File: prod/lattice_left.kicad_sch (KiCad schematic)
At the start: 83 parts, among them J1 USB_C_Receptacle, J2 USB_C_Receptacle, SW1 SW_Push, SW2 SW_Push, U1 XC6206PxxxMR, U2 USBLC6-2SC6, U3 W25Q128JVS, U4 RP2040, Y1 12MHz

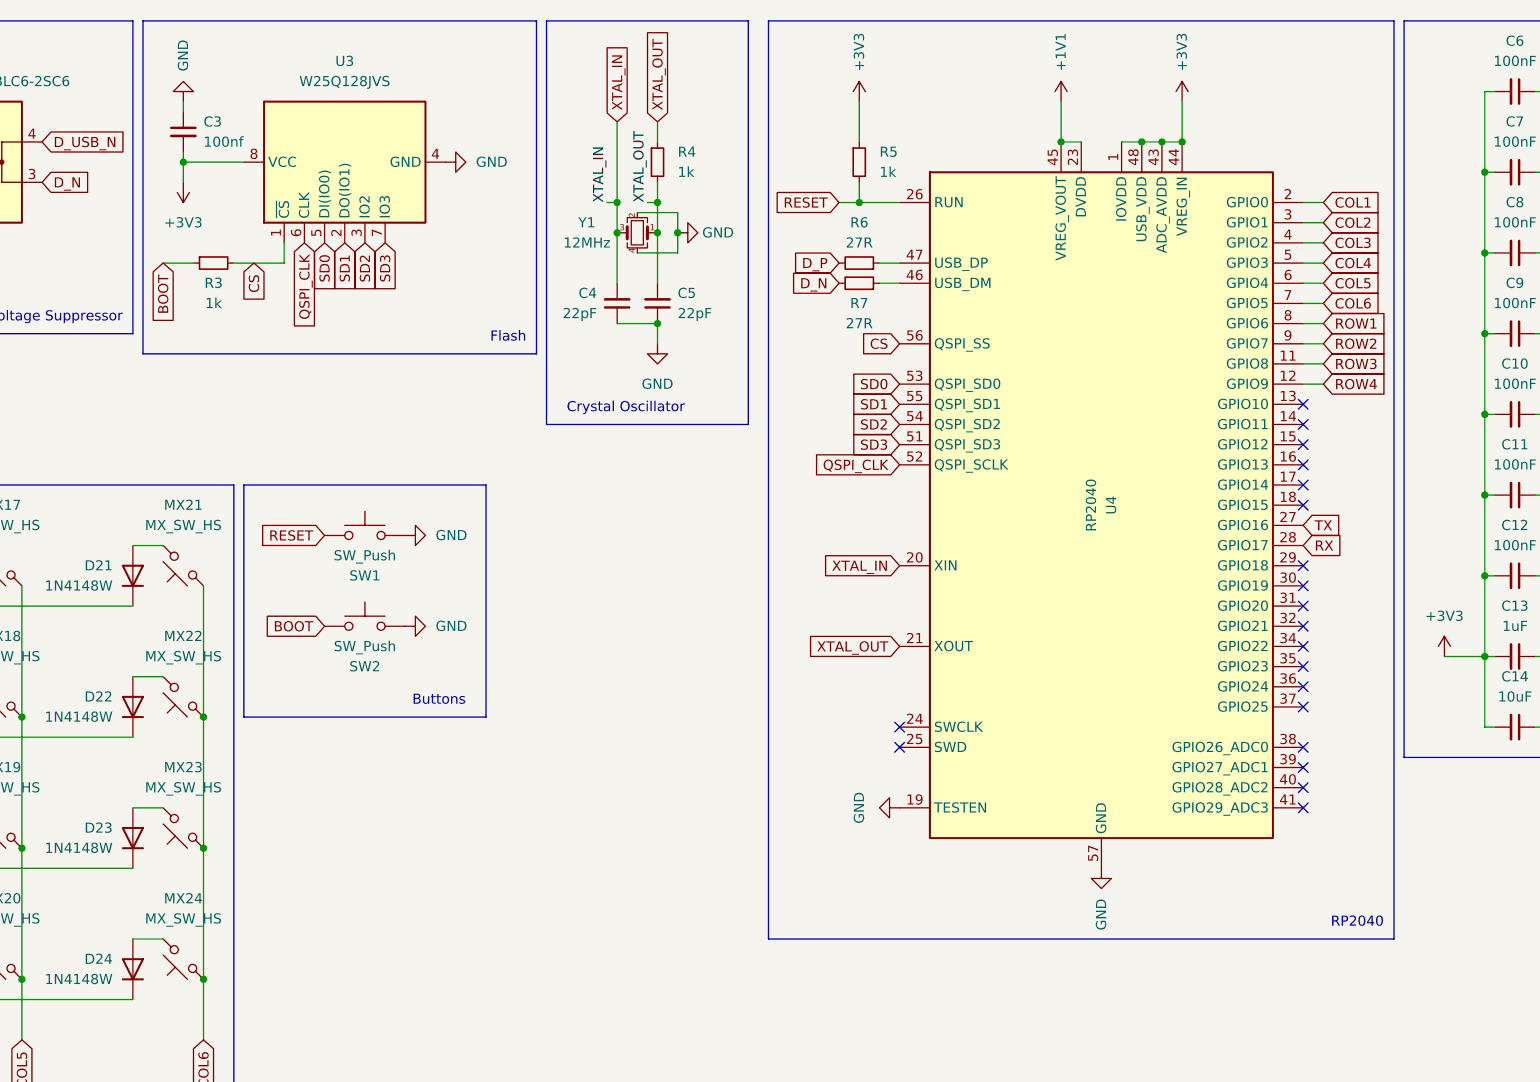
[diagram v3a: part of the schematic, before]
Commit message: component placement (swap rp2040 and flash)
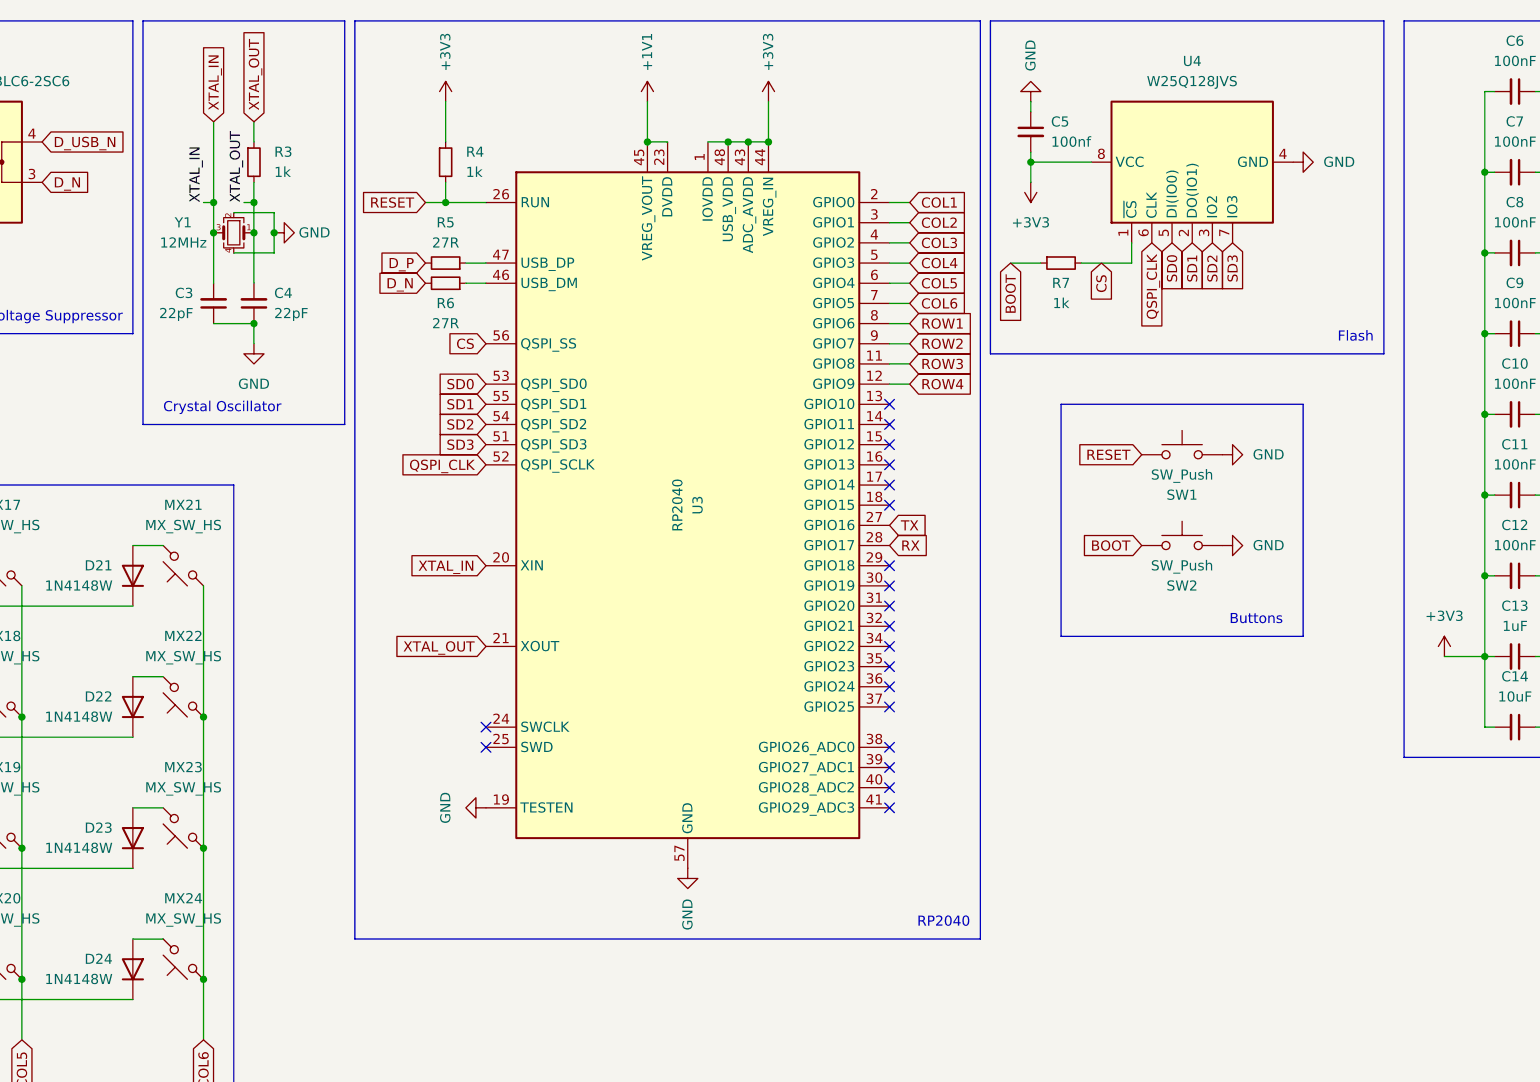
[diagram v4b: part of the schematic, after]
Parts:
- renumbered C4 to C3, C5 to C4, C3 to C5, R4 to R3, R5 to R4, R6 to R5, R7 to R6, R3 to R7, U4 to U3, U3 to U4
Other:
- moved on the sheet: C3, C4, C5, R3, R4, R5, R6, R7, SW1, SW2, U3, U4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
